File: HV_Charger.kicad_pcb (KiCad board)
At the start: 2 copper layers, 31 parts, among them J1 HVIL, J12 Battery GLV, J13 3557-2, J2 E-Stop, J3 PP Connector, J4 IMD Indicator, J5 AMS Indicator, J6 CAN, J7 CAN_Expansion1, J8 CAN_Expansion2, J9 DC Input, Q1 Q_PMOS_SGD

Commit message: more stuff done
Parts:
- moved PAD3 58.5 mm to (56.0, 103.2)
- moved PAD4 22.1 mm to (56.0, 67.4)
- moved J13 9.67 mm to (71.0, 77.4)
- moved PAD6 9.61 mm to (56.0, 76.4)
- moved R2 7.58 mm to (126.2, 75.5), turned to 90 degrees
- moved JP2 7.30 mm to (141.8, 73.2)
- moved J1 6.28 mm to (171.2, 104.9)
- moved PAD5 5.84 mm to (94.0, 109.4)
- moved JP1 4.44 mm to (135.7, 73.2), turned to -90 degrees
- moved J5 3.91 mm to (117.0, 104.9)
- moved J4 3.91 mm to (107.8, 105.1)
- moved PAD1 3.81 mm to (56.0, 92.0)
- moved PAD2 3.40 mm to (78.6, 109.2)
- moved D3 2.98 mm to (126.2, 80.4), turned to 180 degrees
- moved J12 2.15 mm to (141.2, 104.8)
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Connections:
- J12 pad 11: CAN H Bridge -> AMS
- J12 pad 3: Shutdown_CON -> Pilot_OUT
- J12 pad 4: Pilot_OUT -> Shutdown_CON
- J12 pad 6: IMD -> CAN L Bridge
- J12 pad 8: AMS -> CAN H Bridge
- J12 pad 9: CAN L Bridge -> IMD
- J13 pad 1: Net-(J13-Pad1) -> 12V_Charge
- J13 pad 2: Net-(J13-Pad2) -> 12V_Charge
- J13 pad 3: Net-(J13-Pad1) -> 12V_Charge
- J13 pad 4: Net-(J13-Pad2) -> 12V_Charge
- J4 pad 1: 24V -> IMD_LO
- J4 pad 2: IMD_LO -> 24V
- J5 pad 1: 24V -> AMS_LO
- J5 pad 2: AMS_LO -> 24V
- PAD6 pad 1: Net-(J13-Pad1) -> 12V_Charge
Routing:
- net 24V: track 0.00 -> 178.7 mm
- net GND: track 0.00 -> 139.9 mm
- net CAN L: track 0.00 -> 48.5 mm
- net Shutdown_OUT: track 0.00 -> 45.8 mm
- net CAN H: track 0.00 -> 43.5 mm
- net Shutdown_CON: track 0.00 -> 41.5 mm
- net Prox_OUT: track 0.00 -> 34.5 mm
- net Pilot_OUT: track 0.00 -> 33.2 mm
- net IMD_LO: track 0.00 -> 30.5 mm
- net AMS: track 0.00 -> 26.1 mm
- net CAN H Bridge: track 0.00 -> 20.4 mm
- net CAN L Bridge: track 0.00 -> 20.2 mm
- net AMS_LO: track 0.00 -> 20.0 mm
- net IMD: track 0.00 -> 16.2 mm
- net Net-(J9-Pad1): track 0.00 -> 14.7 mm
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- added copper zone on F.Cu, net 12V_Charge
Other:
- board outline added: 157.8 x 54.2 mm

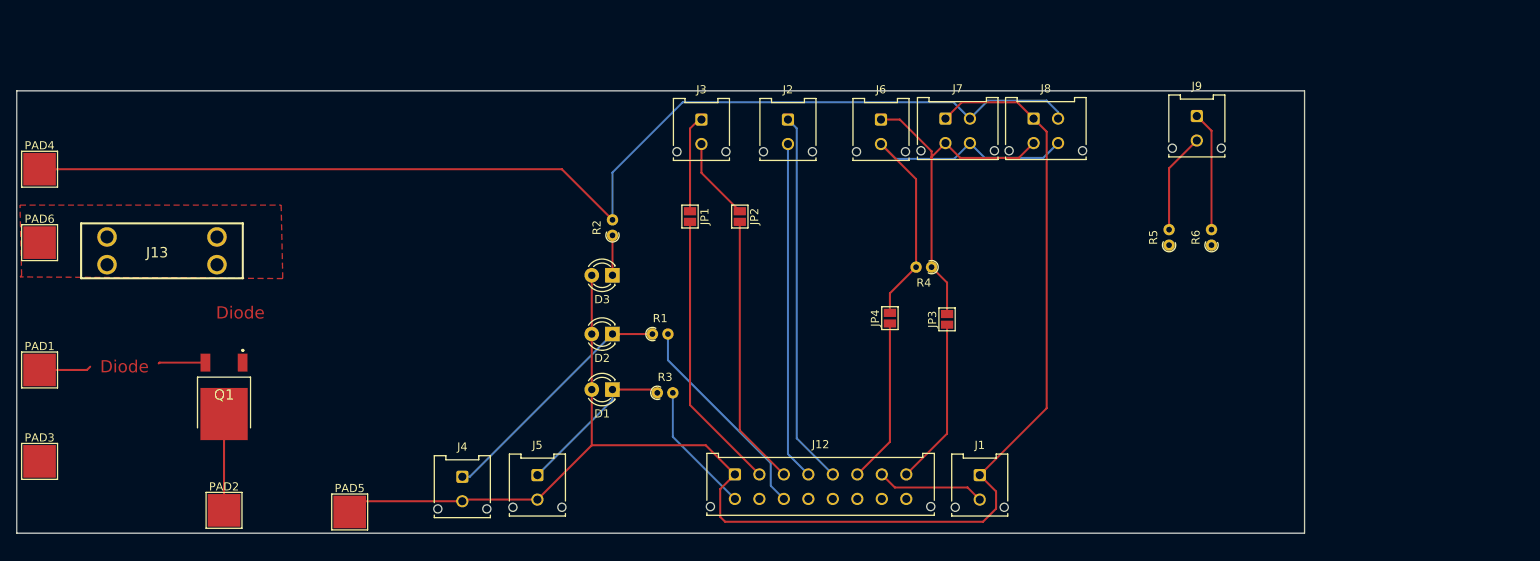
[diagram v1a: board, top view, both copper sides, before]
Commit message: Added more footprints and did layout, banana jack left to do:
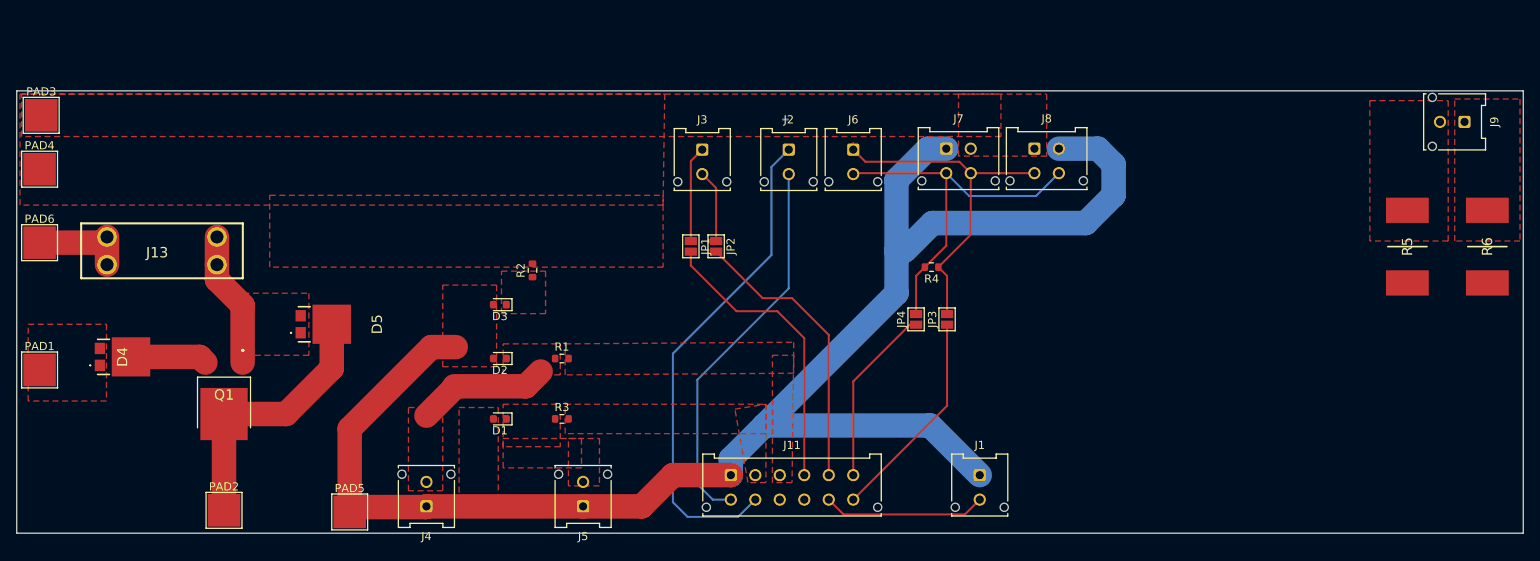
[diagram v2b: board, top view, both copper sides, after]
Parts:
- removed J12: Battery GLV, Connector_Molex:Molex_Micro-Fit_3.0_43045-1612_2x08_P3.00mm_Vertical
- added D4: D_Schottky, SamacSys_Parts:RBQ10RSM10BTL1, F.Cu at (66.2, 90.4)
- added D5: D_Schottky, SamacSys_Parts:RBQ10RSM10BTL1, F.Cu at (90.8, 86.4)
- added J11: Conn_02x06_Top_Bottom, Connector_Molex:Molex_Micro-Fit_3.0_43045-1212_2x06_P3.00mm_Vertical, F.Cu at (140.7, 104.9)
- D1, D2, D3: footprint LED_THT:LED_D3.0mm -> LED_SMD:LED_0603_1608Metric
- R1, R2, R3, R4: footprint Resistor_THT:R_Axial_DIN0204_L3.6mm_D1.6mm_P1.90mm_Vertical -> Resistor_SMD:R_0603_1608Metric
- R5, R6: footprint Resistor_THT:R_Axial_DIN0204_L3.6mm_D1.6mm_P1.90mm_Vertical -> SamacSys_Parts:RESC11050X120N
- moved PAD3 42.4 mm to (56.2, 60.8)
- moved R6 33.8 mm to (233.4, 76.9)
- moved J9 32.8 mm to (230.6, 61.6), turned to -90 degrees
- moved R5 29.2 mm to (223.6, 76.9)
- moved D1 14.3 mm to (112.4, 98.0)
- moved D3 14.3 mm to (112.4, 84.0)
- moved D2 14.1 mm to (112.4, 90.6)
- moved R3 12.1 mm to (120.0, 98.0)
- moved R1 11.5 mm to (120.0, 90.6)
- moved R2 10.7 mm to (116.4, 79.8)
- moved J5 6.78 mm to (122.6, 108.7), turned to 180 degrees
- moved J4 5.70 mm to (103.4, 108.7), turned to 180 degrees
- moved J6 5.01 mm to (155.7, 65.0)
- moved JP2 4.66 mm to (138.9, 76.8)
- moved J2 3.69 mm to (147.8, 65.0)
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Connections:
- net Net-(D5-Pad1) renamed Moss_D_O
- J13 pad 2: 12V_Charge -> Fuse_M_D
- J13 pad 4: 12V_Charge -> Fuse_M_D
- J4 pad 1: IMD_LO -> 24V
- J4 pad 2: 24V -> IMD_LO
- J5 pad 1: AMS_LO -> 24V
- J5 pad 2: 24V -> AMS_LO
- J7 pad 3: CAN H -> CAN L
- J7 pad 4: CAN L -> CAN H
- J8 pad 1: 24V -> GND
- J8 pad 2: GND -> 24V
- PAD1 pad 1: Net-(D4-Pad2) -> D_to_D
- Q1 pad 1: Net-(D5-Pad2) -> Fuse_M_D
- Q1 pad 3: Net-(D4-Pad1) -> D_to_M
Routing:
- net GND: track 139.9 -> 0.00 mm
- net AMS: track 26.1 -> 0.00 mm
- net 24V: track 178.7 -> 199.7 mm
- net Moss_D_O: track 11.8 -> 32.7 mm
- net AMS_LO: track 20.0 -> 0.00 mm
- net Fuse_M_D: track 0.00 -> 16.7 mm
- net IMD: track 16.2 -> 0.28 mm
- net Shutdown_OUT: track 45.8 -> 61.4 mm
- net Net-(J9-Pad1): track 14.7 -> 0.00 mm
- net IMD_LO: track 30.5 -> 16.1 mm
- net Net-(J9-Pad2): track 12.3 -> 0.00 mm
- net 12V_Charge: track 0.00 -> 12.0 mm
- net D_to_M: track 0.00 -> 9.41 mm
- net Shutdown_IN: track 13.3 -> 20.0 mm
- net Net-(D4-Pad2): track 6.37 -> 0.00 mm
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- added copper zone on F.Cu, net 24V
- added copper zone on F.Cu, net AMS
- added copper zone on F.Cu, net AMS_LO
- added copper zone on F.Cu, net D_to_D
- added copper zone on F.Cu, net Fuse_M_D
- added copper zone on F.Cu, net GND
- added copper zone on F.Cu, net IMD
- added copper zone on F.Cu, net IMD_LO
- added copper zone on F.Cu, net Net-(D3-Pad1)
- added copper zone on F.Cu, net Net-(J9-Pad1)
- added copper zone on F.Cu, net Net-(J9-Pad2)
- removed copper zone on F.Cu, net 12V_Charge
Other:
- board size 157.8 x 54.2 mm -> 184.6 x 54.2 mm
- board text removed: "Diode"
